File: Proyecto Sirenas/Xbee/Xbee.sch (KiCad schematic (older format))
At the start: 10 parts

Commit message: bornera de programacion
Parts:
- added D1: Assoc-RSSI, symbol Device:LED_ALT
- added J?: Programación, symbol Connector_Generic:Conn_02x05_Counter_Clockwise
- added J?: Entrada, symbol Connector:Screw_Terminal_01x02
- added J?: Salida, symbol Connector:Screw_Terminal_01x02
- added JP?: Assoc-RSSI, symbol Jumper:Jumper_3_Open
- added Q?: BC338, Package_TO_SOT_THT:TO-92_Inline, symbol Transistor_BJT:BC338
- added R1: 68, symbol Device:R
- added R?: 330, symbol Device:R
- added U? (x3): LM358, symbol Amplifier_Operational:LM358
- U2: renamed from U?; symbol XBP24CZ7PITB003:XBP24CZ7PITB003 -> Xbee-rescue:XBP24CZ7PITB003-XBP24CZ7PITB003
- gave numbers to parts that had none: 9
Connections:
- net labels added: Assoc., CTS, Comm., DSR, DTR, RSSI, RTS, RXD, TXD
- wire segments 21 -> 32
- no-connect marks 1 -> 3
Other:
- moved on the sheet: SW2

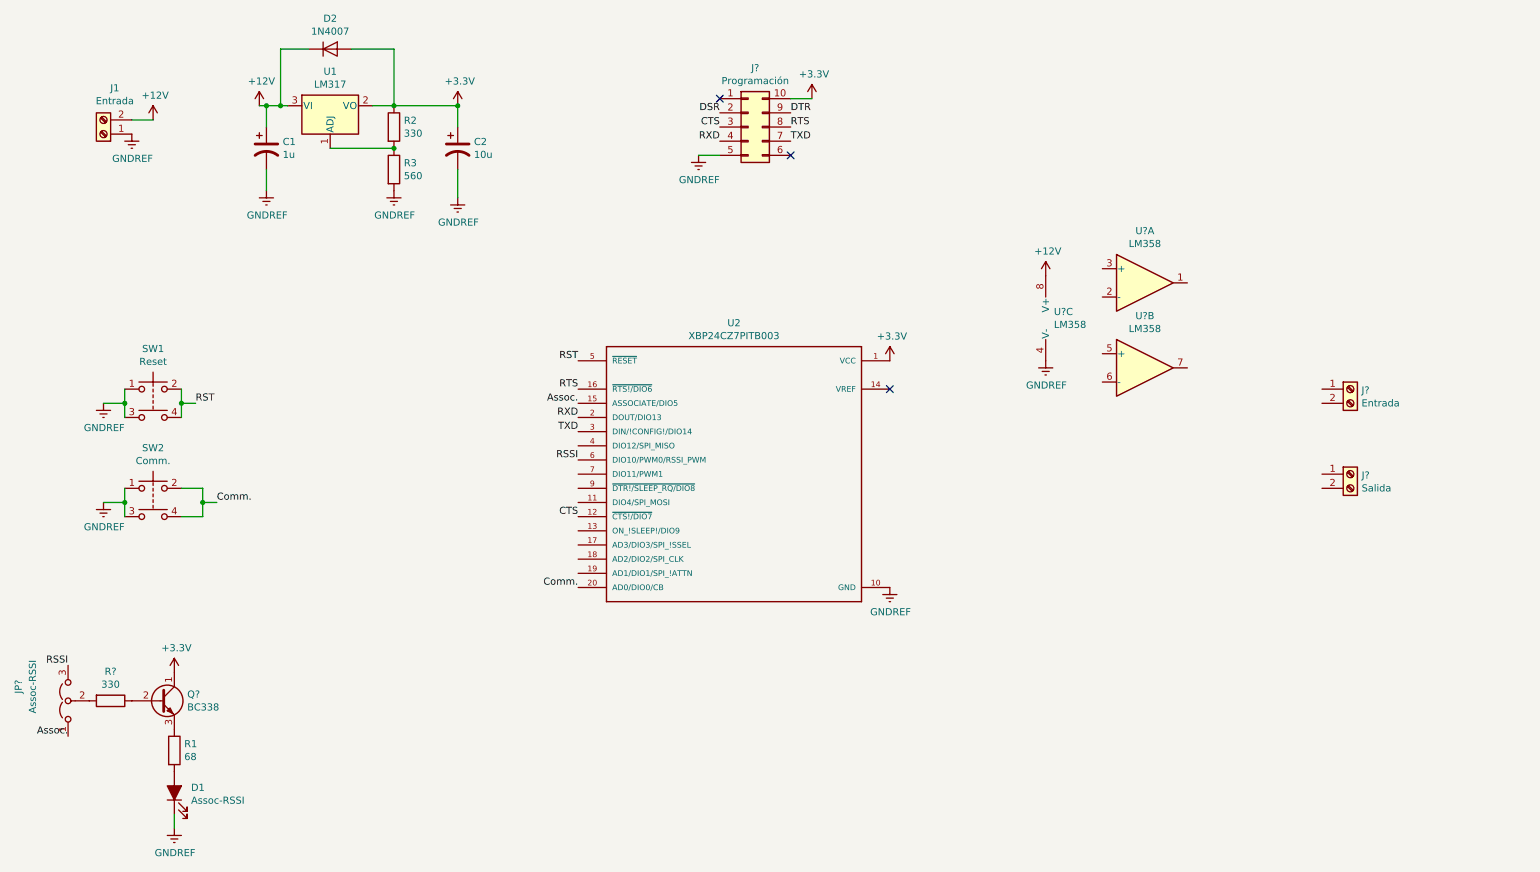
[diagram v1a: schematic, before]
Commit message: Esquematico finalizado
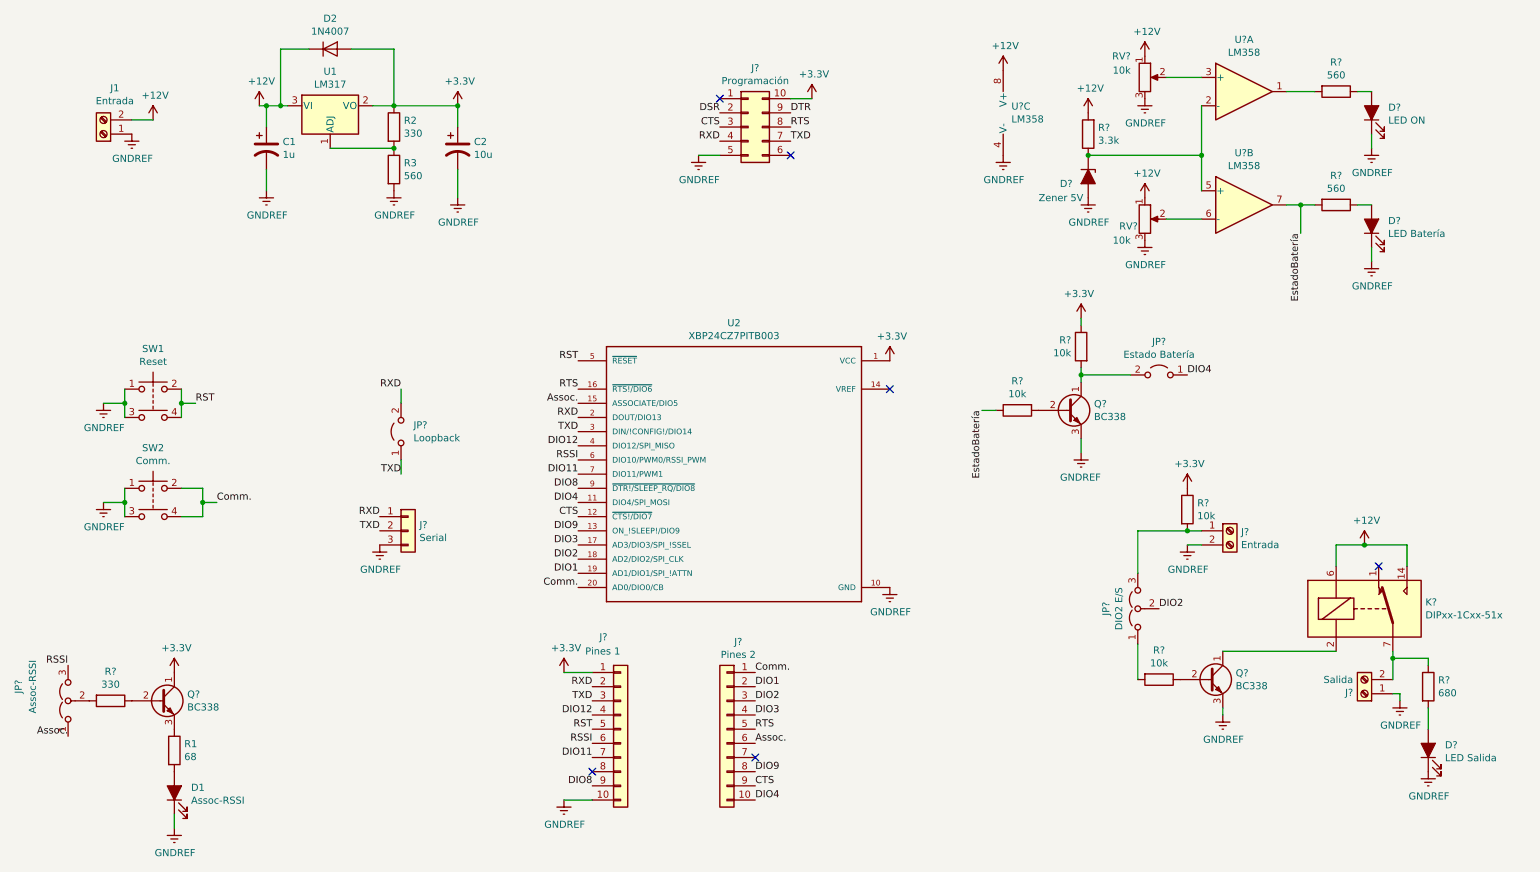
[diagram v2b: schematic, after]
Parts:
- added D?: Zener 5V, symbol Device:D_Zener_ALT
- added D?: LED ON, symbol Device:LED_ALT
- added D?: LED Batería, symbol Device:LED_ALT
- added D?: LED Salida, symbol Device:LED_ALT
- added J?: Pines 1, symbol Connector_Generic:Conn_01x10
- added J?: Pines 2, symbol Connector_Generic:Conn_01x10
- added J?: Serial, symbol Connector_Generic:Conn_01x03
- added JP?: Estado Batería, symbol Jumper:Jumper_2_Open
- added JP?: DIO2 E/S, symbol Jumper:Jumper_3_Open
- added JP?: Loopback, symbol Jumper:Jumper_2_Open
- added K?: DIPxx-1Cxx-51x, Relay_THT:Relay_StandexMeder_DIP_LowProfile, symbol Relay:DIPxx-1Cxx-51x
- added Q? (x2): BC338, Package_TO_SOT_THT:TO-92_Inline, symbol Transistor_BJT:BC338
- added R?: 3.3k, symbol Device:R
- added R? (x2): 560, symbol Device:R
- added R? (x4): 10k, symbol Device:R
- added R?: 680, symbol Device:R
- added RV? (x2): 10k, symbol Device:R_POT
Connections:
- net +12V: now also K?.14, K?.6, R?.2, RV?.1, RV?.1
- net +3V3: now also J?.1 (Pin_1), R?.1, R?.1
- net Assoc.: now also J?.6 (Pin_6)
- net CTS: now also J?.9 (Pin_9)
- net Comm.: now also J?.1 (Pin_1)
- net GNDREF: now also J?.1 (Pin_1), J?.2 (Pin_2), D?.1 (K), D?.1 (K), D?.1 (K), D?.2 (A), J?.10 (Pin_10), J?.3 (Pin_3), Q?.3 (E), Q?.3 (E), RV?.3, RV?.3
- net RSSI: now also J?.6 (Pin_6)
- net RST: now also J?.5 (Pin_5)
- net RTS: now also J?.5 (Pin_5)
- net RXD: now also J?.1 (Pin_1), J?.2 (Pin_2), JP?.2 (B)
- net TXD: now also J?.2 (Pin_2), J?.3 (Pin_3), JP?.1 (A)
- net DIO4: now reaches U2.11 (DIO4/SPI_MOSI)
- net DIO4: now also J?.10 (Pin_10), JP?.1 (A)
- net DIO9: now reaches U2.13 (ON_!SLEEP!/DIO9)
- net DIO9: now also J?.8 (Pin_8)
- net DIO3: now reaches U2.17 (AD3/DIO3/SPI_!SSEL)
- net DIO3: now also J?.4 (Pin_4)
- net DIO2: now reaches U2.18 (AD2/DIO2/SPI_CLK)
- net DIO2: now also J?.3 (Pin_3), JP?.2 (C)
- net DIO1: now reaches U2.19 (AD1/DIO1/SPI_!ATTN)
- net DIO1: now also J?.2 (Pin_2)
- net DIO12: now reaches U2.4 (DIO12/SPI_MISO)
- net DIO12: now also J?.4 (Pin_4)
- net DIO11: now reaches U2.7 (DIO11/PWM1)
- net DIO11: now also J?.7 (Pin_7)
- net DIO8: now reaches U2.9 (~DTR!/SLEEP_RQ/DIO8~)
- net DIO8: now also J?.9 (Pin_9)
- net at J?.1 (Pin_1): now also JP?.3 (B), R?.2
- net at J?.2 (Pin_2): now also K?.7, K?.8, R?.1
- net at U?.1: now also R?.2
- net at U?.2 (-): now also U?.5 (+), D?.1 (K), R?.1
- net at U?.3 (+): now also RV?.2
- net at U?.6 (-): now also RV?.2
- net EstadoBatería: now reaches U?.7
- net EstadoBatería: now also R?.1, R?.2
- new net: D?.2 (A), R?.1 (x2)
- new net: JP?.2 (B), Q?.1 (C), R?.2
- new net: Q?.2 (B), R?.2
- new net: JP?.1 (A), R?.2
- new net: K?.2, Q?.1 (C)
- new net: Q?.2 (B), R?.1
- new net: D?.2 (A), R?.2
- no-connect marks 3 -> 6
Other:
- moved on the sheet: J?, U?A, U?B, U?C

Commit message: Esquematico finalizado con diodo
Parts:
- added D?: 1N4007, Diode_THT:D_DO-41_SOD81_P10.16mm_Horizontal, symbol Diode:1N4007
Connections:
- net +12V: now also D?.1 (K)
- net at K?.2, Q?.1 (C): now also D?.2 (A)
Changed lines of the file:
@@
 P 9150 4300
 F 0 "J?" H 9229 4292 50  0000 L CNN
-F 1 "Entrada" H 9229 4201 50  0000 L CNN
+F 1 "Entrada" H 9050 4100 50  0000 L CNN
 F 2 "" H 9150 4300 50  0001 C CNN
 F 3 "~" H 9150 4300 50  0001 C CNN
@@
 Connection ~ 10100 4400
 Wire Wire Line
-	9100 5150 9900 5150
+	9100 5150 9450 5150
 Wire Wire Line
 	9100 5550 9100 5600
@@
 DIO3
 NoConn ~ 5800 5900
+$Comp
+L Diode:1N4007 D?
+U 1 1 5C1AA185
+P 9450 4850
+F 0 "D?" V 9404 4929 50  0000 L CNN
+F 1 "1N4007" V 9495 4929 50  0000 L CNN
+F 2 "Diode_THT:D_DO-41_SOD81_P10.16mm_Horizontal" H 9450 4675 50  0001 C CNN
+F 3 "http://www.vishay.com/docs/88503/1n4001.pdf" H 9450 4850 50  0001 C CNN
+	1    9450 4850
+	0    1    1    0
+$EndComp
+Wire Wire Line
+	9450 4700 9450 4400
+Wire Wire Line
+	9450 4400 9900 4400
+Connection ~ 9900 4400
+Wire Wire Line
+	9450 5000 9450 5150
+Connection ~ 9450 5150
+Wire Wire Line
+	9450 5150 9900 5150
 $EndSCHEMATC

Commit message: Esquematico agregado de pulldown-conexiones Raspberry
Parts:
- removed J?: Serial, symbol Connector_Generic:Conn_01x03
- added J2: Conn_01x05, symbol Connector_Generic:Conn_01x05
- added R8: 10k, symbol Device:R
- gave numbers to parts that had none: 30
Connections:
- net GNDREF: now also J2.5 (Pin_5), R8.2
- net RXD: now also J2.3 (Pin_3)
- net TXD: now also J2.4 (Pin_4)
- net Rasp.In: now reaches J6.1 (Pin_1), JP3.3 (B), R10.2
- net Rasp.In: now also J2.1 (Pin_1)
- net Rasp.Out: now reaches JP3.1 (A), R9.2
- net Rasp.Out: now also J2.2 (Pin_2), R8.1
